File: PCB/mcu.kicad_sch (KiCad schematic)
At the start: 35 parts, among them J1 STDC-14 Debug, Q1 2N7002, SW1 Reset, U1 ADM1818, U2 W25N512GVEIG, U3 STM32G473RCTx, Y1 16MHz/8pF

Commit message: Generate project from template
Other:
- title: template_pretty_name -> EOS Homework Board
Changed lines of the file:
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@@
 	(paper "A4")
 	(title_block
-		(title "template_pretty_name")
+		(title "EOS Homework Board")
 	)
 	(text "512Mb NAND Flash"

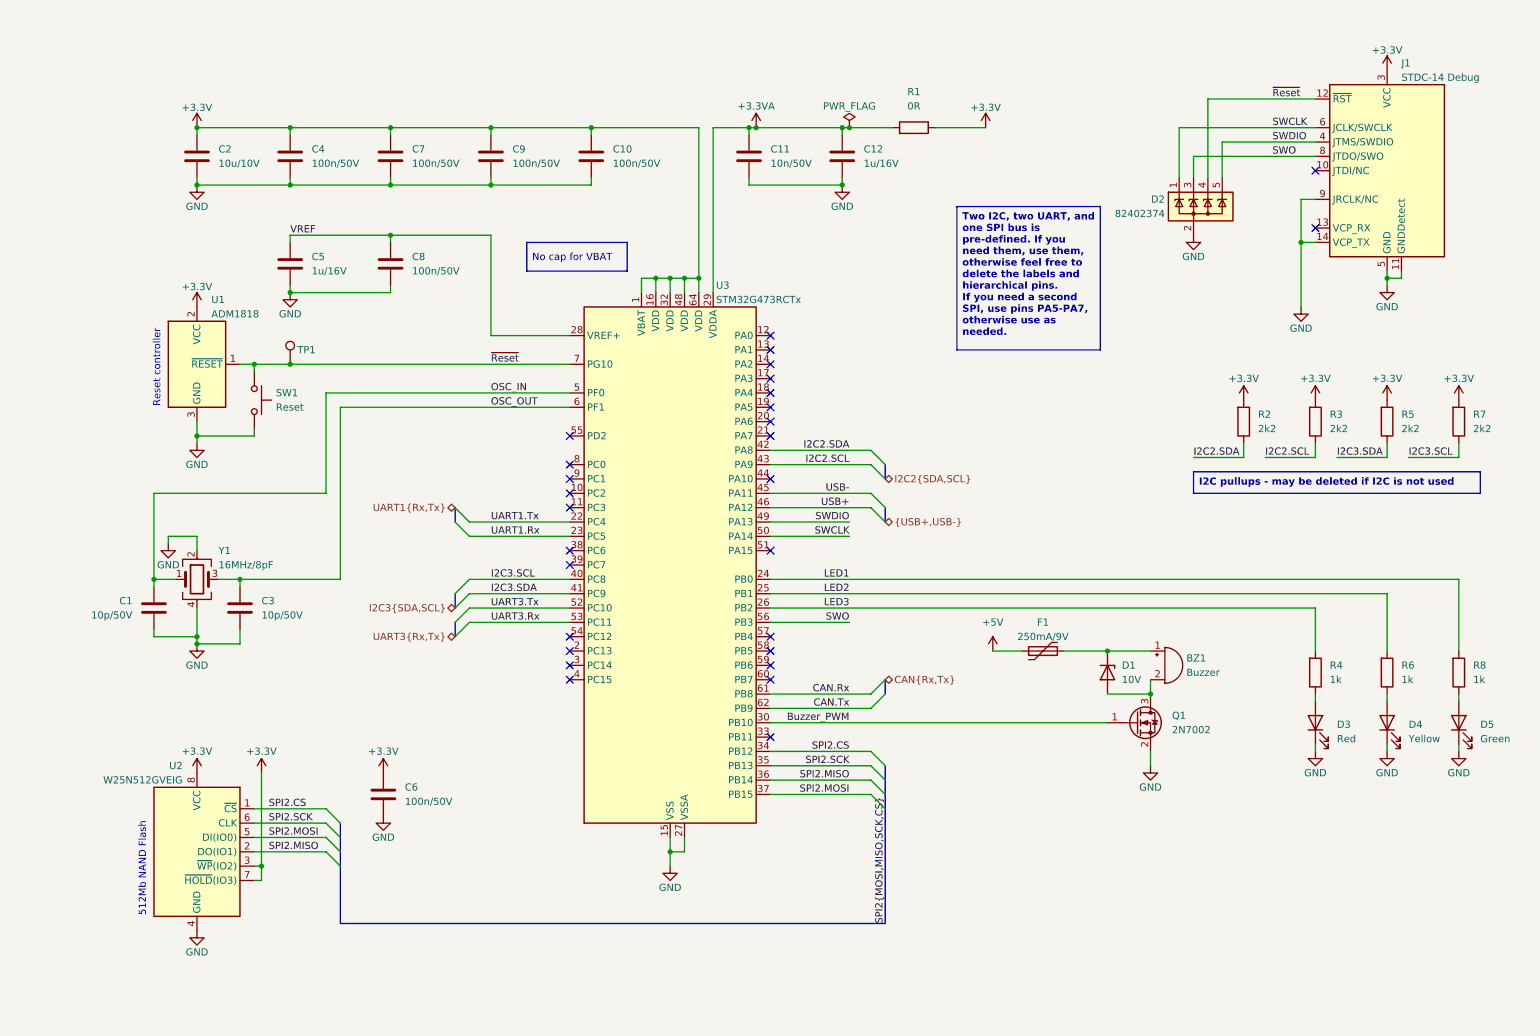
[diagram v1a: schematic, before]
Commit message: Schematic done
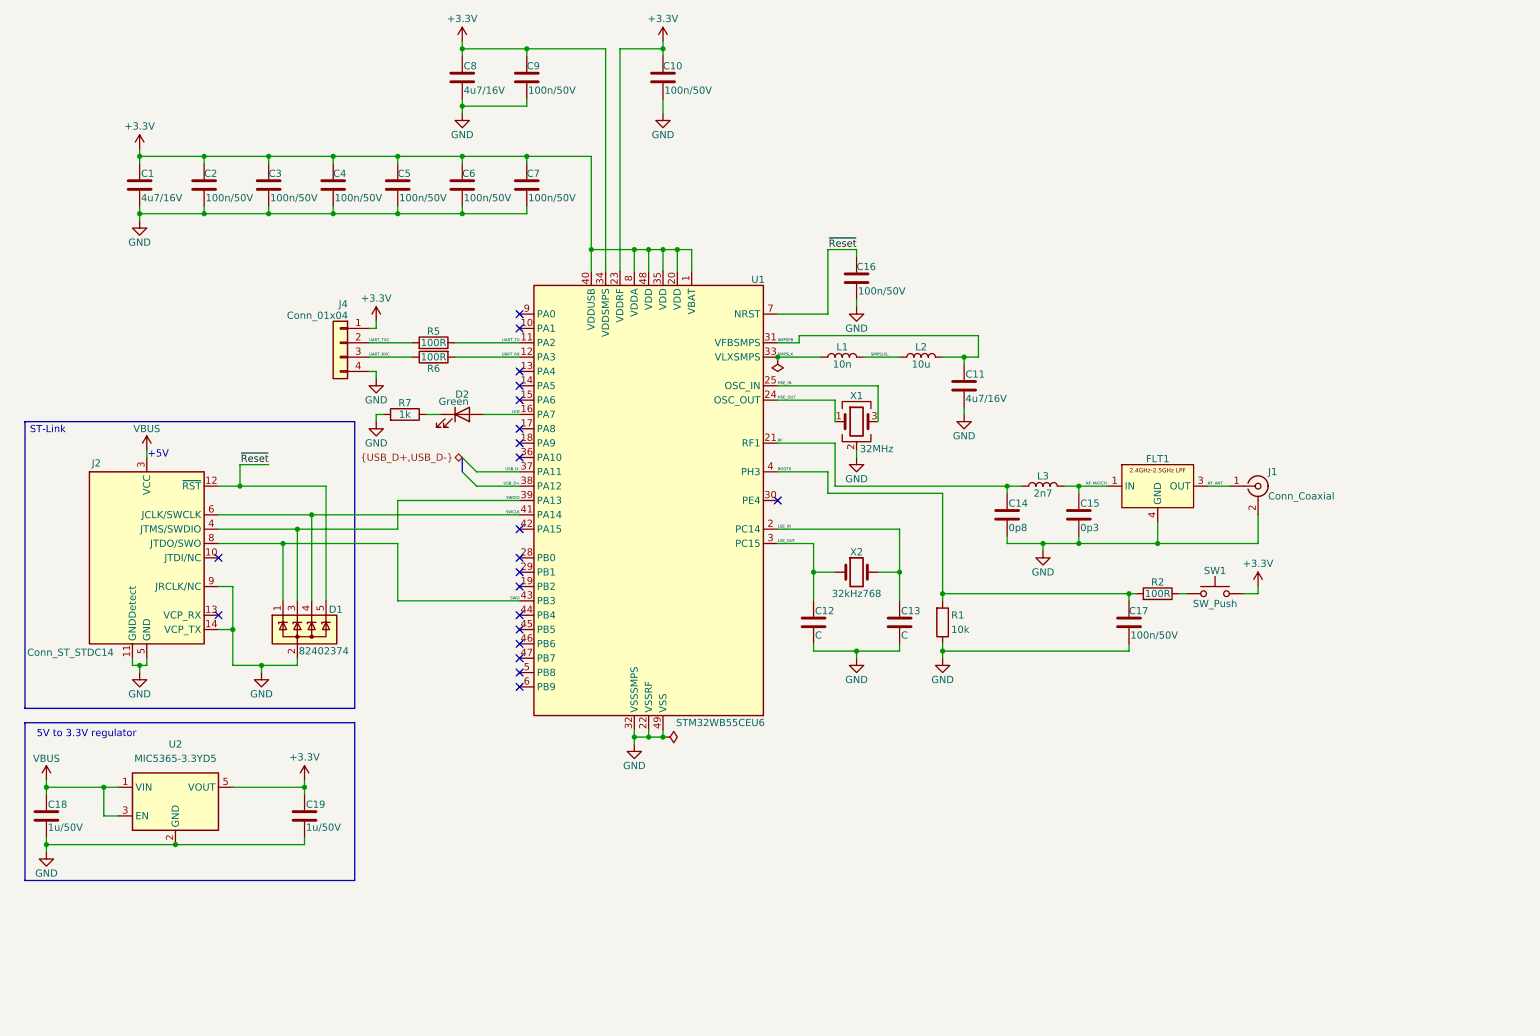
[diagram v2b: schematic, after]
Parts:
- removed BZ1: Buzzer, kicad-standard-lib:Buzzer_CUI_CMT-8504-100-SMT-TR, symbol kicad-standard-lib:Buzzer_CUI_CMT-8504-100-SMT-TR
- removed C1, C3: 10p/50V, Capacitor_SMD:C_0603_1608Metric, symbol kicad-standard-lib:C_10p
- removed C11: 10n/50V, Capacitor_SMD:C_0603_1608Metric, symbol kicad-standard-lib:C_10n
- removed C12, C5: 1u/16V, Capacitor_SMD:C_0603_1608Metric, symbol kicad-standard-lib:C_1u_16V
- removed C2: 10u/10V, Capacitor_SMD:C_0805_2012Metric, symbol kicad-standard-lib:C_10u
- removed C8: 100n/50V, Capacitor_SMD:C_0603_1608Metric, symbol kicad-standard-lib:C_100n
- removed D1: 10V, Diode_SMD:D_SOD-523, symbol kicad-standard-lib:D_Zener_10v
- removed D2: 82402374, Package_TO_SOT_SMD:SOT-353_SC-70-5, symbol kicad-standard-lib:D_TVSx4
- removed D3: Red, LED_SMD:LED_0603_1608Metric, symbol kicad-standard-lib:LED_Red
- removed D4: Yellow, LED_SMD:LED_0603_1608Metric, symbol kicad-standard-lib:LED_Yellow
- removed D5: Green, LED_SMD:LED_0603_1608Metric, symbol kicad-standard-lib:LED_Green
- removed F1: 250mA/9V, Fuse:Fuse_0603_1608Metric, symbol kicad-standard-lib:F_250mA_9V
- removed J1: STDC-14 Debug, kicad-standard-lib:IDC-Header_2x07_P1.27mm_Vertical_SMD, symbol Connector:Conn_ST_STDC14
- removed Q1: 2N7002, Package_TO_SOT_SMD:SOT-23, symbol kicad-standard-lib:Q_2N7002
- removed R1: 0R, Resistor_SMD:R_0603_1608Metric, symbol kicad-standard-lib:R_0R
- removed R2, R3, R5, R7: 2k2, Resistor_SMD:R_0603_1608Metric, symbol kicad-standard-lib:R_2k2
- removed R4, R6, R8: 1k, Resistor_SMD:R_0603_1608Metric, symbol kicad-standard-lib:R_1k
- removed SW1: Reset, kicad-standard-lib:SW_Push_Wuerth_434123025826, symbol kicad-standard-lib:SW_Pushbutton
- removed TP1: TestPoint, TestPoint:TestPoint_THTPad_D2.0mm_Drill1.0mm, symbol Connector:TestPoint
- removed U1: ADM1818, Package_TO_SOT_SMD:SOT-23, symbol kicad-standard-lib:ADM1818
- removed U2: W25N512GVEIG, kicad-standard-lib:WSON-8-1EP_8x6mm_P1.27mm_EP3.4x4.3mm, symbol kicad-standard-lib:W25N512GVEIG
- removed U3: STM32G473RCTx, Package_QFP:LQFP-64_10x10mm_P0.5mm, symbol MCU_ST_STM32G4:STM32G473RCTx
- removed Y1: 16MHz/8pF, Crystal:Crystal_SMD_3225-4Pin_3.2x2.5mm, symbol kicad-standard-lib:Crystal_16MHz
- added C1, C11, C8: 4u7/16V, Capacitor_SMD:C_0805_2012Metric, symbol kicad-standard-lib:C_4u7
- added C12, C13: C, symbol Device:C
- added C14: 0p8, symbol Device:C
- added C15: 0p3, symbol Device:C
- added C16, C17, C2, C3, C5: 100n/50V, Capacitor_SMD:C_0603_1608Metric, symbol kicad-standard-lib:C_100n
- added C18, C19: 1u/50V, Capacitor_SMD:C_0603_1608Metric, symbol kicad-standard-lib:C_1u_50V
- added D1: 82402374, Package_TO_SOT_SMD:SOT-353_SC-70-5, symbol kicad-standard-lib:D_TVSx4
- added D2: Green, LED_SMD:LED_0603_1608Metric, symbol kicad-standard-lib:LED_Green
- added FLT1: DLF162500LT-5028A1, OzelHD-addition-repo_FP:DLF162500LT-5028A1, symbol OzelHD-addition-repo:DLF162500LT-5028A1
- added J1: Conn_Coaxial, symbol Connector:Conn_Coaxial
- added J2: Conn_ST_STDC14, kicad-standard-lib:IDC-Header_2x07_P1.27mm_Vertical_SMD, symbol Connector:Conn_ST_STDC14
- added J4: Conn_01x04, symbol Connector_Generic:Conn_01x04
- added L1: 10n, symbol Device:L
- added L2: 10u, symbol Device:L
- added L3: 2n7, symbol Device:L
- added R1: 10k, Resistor_SMD:R_0603_1608Metric, symbol kicad-standard-lib:R_10k
- added R2, R5, R6: 100R, Resistor_SMD:R_0603_1608Metric, symbol kicad-standard-lib:R_100R
- added R7: 1k, Resistor_SMD:R_0603_1608Metric, symbol kicad-standard-lib:R_1k
- added SW1: SW_Push, symbol Switch:SW_Push
- added U1: STM32WB55CEU6, Package_DFN_QFN:QFN-48-1EP_7x7mm_P0.5mm_EP5.6x5.6mm, symbol MCU_ST_STM32WB:STM32WB55CEUx
- added U2: MIC5365-3.3YD5, Package_TO_SOT_SMD:TSOT-23-5, symbol Regulator_Linear:MIC5365-3.3YD5
- added X1: 32MHz, symbol Device:Crystal_GND24
- added X2: 32kHz768, symbol Device:Crystal
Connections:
- net +3.3V: now also C1.1, C19.1, C2.1, C3.1, C5.1, C8.1, J4.1 (Pin_1), SW1.2, U1.1 (VBAT), U1.20 (VDD), U1.23 (VDDRF), U1.34 (VDDSMPS), U1.35 (VDD), U1.40 (VDDUSB), U1.48 (VDD), U1.8 (VDDA), U2.5 (VOUT)
- net GND: now also C1.2, C11.2, C12.2, C13.2, C14.2, C15.2, C16.2, C17.2, C18.2, C19.2, C2.2, C3.2, C5.2, C8.2, D1.2 (A), FLT1.2 (GND), FLT1.4 (GND), J1.2 (Ext), J2.11 (GNDDetect), J2.14 (VCP_TX), J2.5 (GND), J2.7 (GND), J2.9 (JRCLK/NC), J4.4 (Pin_4), R1.2, R7.1, U1.22 (VSSRF), U1.32 (VSSSMPS), U1.49 (VSS), U2.2 (GND), X1.2 (G), X1.4 (G)
- net SWCLK: now also D1.4 (K), J2.6 (JCLK/SWCLK), U1.41 (PA14)
- net SWDIO: now also D1.3 (K), J2.4 (JTMS/SWDIO), U1.39 (PA13)
- net SWO: now also D1.1 (K), J2.8 (JTDO/SWO), U1.43 (PB3)
- net ~{Reset}: now also C16.1, D1.5 (K), J2.12 (~{RST}), U1.7 (NRST)
- new net: D2.1 (K), R7.2
- new net: R2.2, SW1.1
- new net BOOT0: C17.1, R1.1, R2.1, U1.4 (PH3)
- new net HSE_IN: U1.25 (OSC_IN), X1.3
- new net HSE_OUT: U1.24 (OSC_OUT), X1.1
- new net LED: D2.2 (A), U1.16 (PA7)
- new net LSE_IN: C13.1, U1.2 (PC14), X2.2
- new net LSE_OUT: C12.1, U1.3 (PC15), X2.1
- new net RF: C14.1, L3.1, U1.21 (RF1)
- new net RF_ANT: FLT1.3 (OUT), J1.1 (In)
- new net RF_MATCH: C15.1, FLT1.1 (IN), L3.2
- new net SMPSFB: C11.1, L2.2, U1.31 (VFBSMPS)
- new net SMPSLX: L1.1, U1.33 (VLXSMPS)
- new net SMPSLXL: L1.2, L2.1
- new net UART_RX: R6.1, U1.12 (PA3)
- new net UART_RXC: J4.3 (Pin_3), R6.2
- new net UART_TX: R5.2, U1.11 (PA2)
- new net UART_TXC: J4.2 (Pin_2), R5.1
- new net USB_D+: U1.38 (PA12)
- new net USB_D-: U1.37 (PA11)
- new net VBUS: C18.1, J2.3 (VCC), U2.1 (VIN), U2.3 (EN)
- no-connect marks 28 -> 21
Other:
- note added: "+5V"
- note added: "5V to 3.3V regulator"
- note added: "ST-Link"
- note removed: "512Mb NAND Flash"
- note removed: "Reset controller"

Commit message: PCB done.
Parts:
- removed C18: 1u/50V, Capacitor_SMD:C_0603_1608Metric, symbol kicad-standard-lib:C_1u_50V
- removed R7: 1k, Resistor_SMD:R_0603_1608Metric, symbol kicad-standard-lib:R_1k
- removed SW1: SW_Push, symbol Switch:SW_Push
- added C15: 1u/50V, Capacitor_SMD:C_0603_1608Metric, symbol kicad-standard-lib:C_1u_50V
- added D3, D4: Red, LED_SMD:LED_0603_1608Metric, symbol kicad-standard-lib:LED_Red
- added FID1, FID2, FID3: Fiducial, Fiducial:Fiducial_1mm_Mask2mm, symbol Mechanical:Fiducial
- added H1, H2, H3, H4: MountingHole_Pad, MountingHole:MountingHole_2.2mm_M2_Pad_Via, symbol Mechanical:MountingHole_Pad
- added J4: USB-C MCU, Connector_USB:USB_C_Receptacle_GCT_USB4105-xx-A_16P_TopMnt_Horizontal, symbol Connector:USB_C_Receptacle_USB2.0_16P
- added R1, R8, R9: 1k, Resistor_SMD:R_0603_1608Metric, symbol kicad-standard-lib:R_1k
- added R6, R7: 5k1, Resistor_SMD:R_0603_1608Metric, symbol kicad-standard-lib:R_5k1
- added SW1: Reset, kicad-standard-lib:SW_Push_Wuerth_434123025826, symbol kicad-standard-lib:SW_Pushbutton
- added TP1, TP2: TestPoint, TestPoint:TestPoint_Pad_D1.0mm, symbol Connector:TestPoint
- added TP3: TestPoint_Square, TestPoint:TestPoint_THTPad_1.5x1.5mm_Drill0.7mm, symbol Connector:TestPoint_Square
- added U3: USBLC6-2SC6, Package_TO_SOT_SMD:SOT-23-6, symbol Power_Protection:USBLC6-2SC6
- C11: renamed from C12; value C -> 10p; footprint (none) -> Capacitor_SMD:C_0603_1608Metric
- C13: value C -> 10p; footprint (none) -> Capacitor_SMD:C_0603_1608Metric
- C16: renamed from C14; footprint (none) -> Capacitor_SMD:C_0603_1608Metric
- C17: renamed from C15; footprint (none) -> Capacitor_SMD:C_0603_1608Metric
- J2: renamed from J4; footprint (none) -> Connector_Molex:Molex_PicoBlade_53048-0410_1x04_P1.25mm_Horizontal
- J3: renamed from J1; footprint (none) -> Connector_Coaxial:U.FL_Hirose_U.FL-R-SMT-1_Vertical
- L1, L3: footprint (none) -> Inductor_SMD:L_0402_1005Metric
- L2: footprint (none) -> Inductor_SMD:L_0805_2012Metric
- X1: footprint (none) -> Crystal:Crystal_SMD_2016-4Pin_2.0x1.6mm; Manifacturer (none) -> NDK
- X2: footprint (none) -> Crystal:Crystal_SMD_2012-2Pin_2.0x1.2mm; Distributor Link (none) -> https://mou.sr/46MWGQP; Manifacturer (none) -> NDK; Manifacturer Part Number (none) -> STDMUB1-32.768K
- renumbered C16 to C12, C11 to C14, C17 to C18, C8 to C6, C6 to C7, C9 to C8, C7 to C9, J2 to J1, R5 to R2, R6 to R3, R1 to R4, R2 to R5
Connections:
- net +3.3V: now also J1.3 (VCC), R9.2, SW1.2, TP2.1
- net GND: now also D2.1 (K), C15.2, D3.1 (K), D4.1 (K), H1.1, H2.1, H3.1, H4.1, J4.A1 (GND), J4.A12 (GND), J4.B1 (GND), J4.B12 (GND), R6.1, R7.1, TP3.1, U3.2 (GND)
- net LED: now also R1.2; no longer D2.2 (A)
- net USB_D+: now also U3.1 (I/O1)
- net USB_D-: now also U3.3 (I/O2)
- net VBUS: now also C15.1, J4.A4 (VBUS), J4.A9 (VBUS), J4.B4 (VBUS), J4.B9 (VBUS), R8.2, TP1.1, U3.5 (VBUS); no longer J1.3 (VCC)
- net at R5.2: now also SW1.1
- net ~{Reset} renamed SW_~{Reset}
- new net: D2.2 (A), R1.1
- new net: J4.A5 (CC1), R6.2
- new net: J4.B5 (CC2), R7.2
- new net: D4.2 (A), R9.1
- new net: D3.2 (A), R8.1
- new net xUSB+: J4.A6 (D+), J4.B6 (D+), U3.6 (I/O1)
- new net xUSB-: J4.A7 (D-), J4.B7 (D-), U3.4 (I/O2)
- no-connect marks 21 -> 24
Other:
- note added: "Boot0 Switch"
- note added: "RF"
- note added: "USB Connector"
- note removed: "+5V"
- moved on the sheet: C12, C16, C17, C18, FLT1, J3, L3, R4, R5
